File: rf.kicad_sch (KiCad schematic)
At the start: 1 part, among them U3 RFM95W-868S2

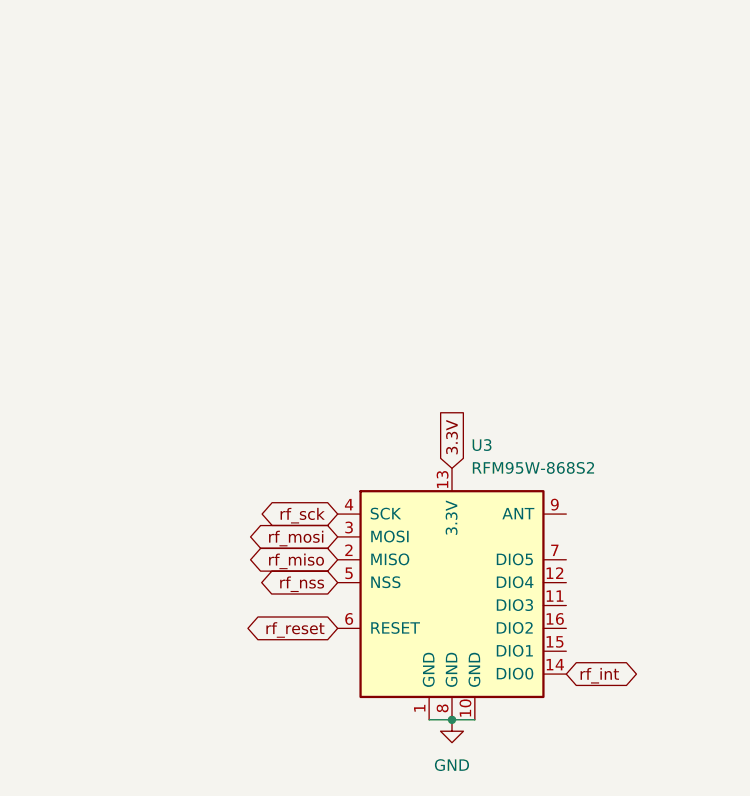
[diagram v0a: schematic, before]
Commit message: Overhaul
Overhauled the schematic so all the components are correct, rewired power to be 12 V instead of 9 V and connected hierarchical labels between modules. Added more decoupling capacitors where they were missing.
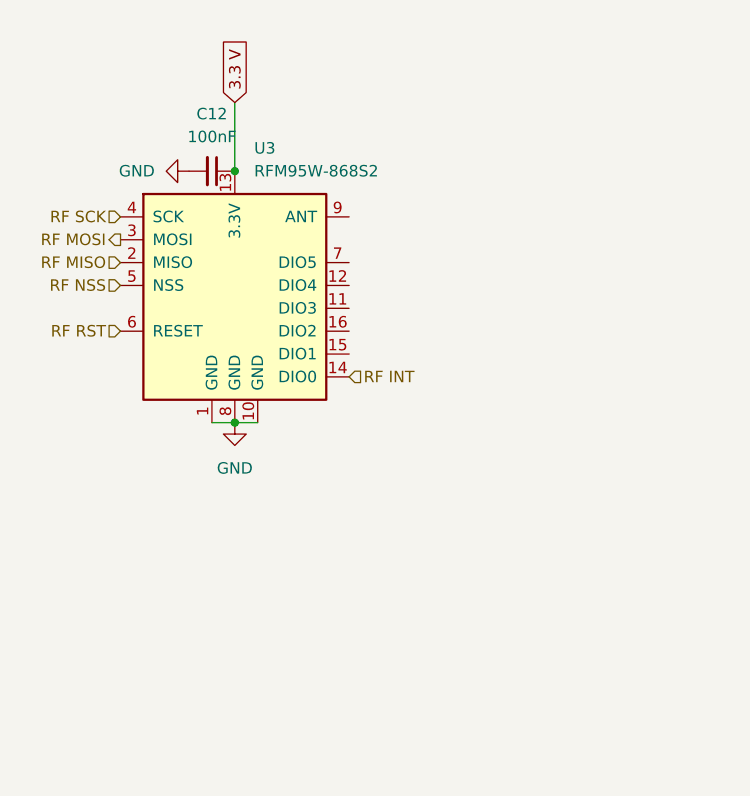
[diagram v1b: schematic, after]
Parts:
- added C12: 100nF, symbol Device:C_Small
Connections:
- net GND: now also C12.2
- net 3.3V renamed 3.3 V
- net 3.3 V: now also C12.1
- net rf_int renamed RF INT
- net rf_miso renamed RF MISO
- net rf_mosi renamed RF MOSI
- net rf_nss renamed RF NSS
- net rf_reset renamed RF RST
- net rf_sck renamed RF SCK
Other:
- moved on the sheet: U3

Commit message: Clean up
Minor fixes to mistakes in the schematic
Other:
- moved on the sheet: C12, U3
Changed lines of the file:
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@@
 	(paper "A4")
 	(junction
-		(at 41.91 57.15)
+		(at 41.91 60.96)
 		(diameter 0)
 		(color 0 0 0 0)
 	)
 	(junction
-		(at 41.91 29.21)
+		(at 41.91 31.75)
 		(diameter 0)
 		(color 0 0 0 0)
@@
 	(wire
 		(pts
-			(xy 41.91 21.59) (xy 41.91 29.21)
+			(xy 41.91 24.13) (xy 41.91 31.75)
 		)
 		(stroke
@@
 	(wire
 		(pts
-			(xy 39.37 57.15) (xy 41.91 57.15)
+			(xy 39.37 60.96) (xy 41.91 60.96)
 		)
 		(stroke
@@
 	(wire
 		(pts
-			(xy 41.91 57.15) (xy 44.45 57.15)
+			(xy 41.91 31.75) (xy 41.91 33.02)
 		)
 		(stroke
@@
 		)
 	)
+	(wire
+		(pts
+			(xy 41.91 60.96) (xy 44.45 60.96)
+		)
+		(stroke
+			(width 0)
+			(type default)
+		)
+	)
 	(global_label "3.3 V"
 		(shape input)
-		(at 41.91 21.59 90)
+		(at 41.91 24.13 90)
 		(fields_autoplaced yes)
 		(effects
@@
 		)
 		(property "Intersheetrefs" "${INTERSHEET_REFS}"
-			(at 41.91 13.5248 90)
+			(at 41.91 16.0648 90)
 			(hide yes)
 			(show_name no)
@@
 	(hierarchical_label "RF NSS"
 		(shape input)
-		(at 29.21 41.91 180)
+		(at 29.21 45.72 180)
 		(effects
 			(font
@@
 	(hierarchical_label "RF SCK"
 		(shape input)
-		(at 29.21 34.29 180)
+		(at 29.21 38.1 180)
 		(effects
 			(font
@@
 	(hierarchical_label "RF MISO"
 		(shape input)
-		(at 29.21 39.37 180)
+		(at 29.21 43.18 180)
 		(effects
 			(font
@@
 	(hierarchical_label "RF MOSI"
 		(shape output)
-		(at 29.21 36.83 180)
+		(at 29.21 40.64 180)
 		(effects
 			(font
@@
 	(hierarchical_label "RF INT"
 		(shape input)
-		(at 54.61 52.07 0)
+		(at 54.61 55.88 0)
 		(effects
 			(font
@@
 	(hierarchical_label "RF RST"
 		(shape input)
-		(at 29.21 46.99 180)
+		(at 29.21 50.8 180)
 		(effects
 			(font
@@
 	(symbol
 		(lib_id "Device:C_Small")
-		(at 39.37 29.21 270)
+		(at 39.37 31.75 270)
 		(unit 1)
 		(body_style 1)
@@
 		(fields_autoplaced yes)
 		(property "Reference" "C12"
-			(at 39.3636 22.86 90)
+			(at 39.3636 25.4 90)
 			(show_name no)
 			(do_not_autoplace no)
@@
 		)
 		(property "Value" "100nF"
-			(at 39.3636 25.4 90)
+			(at 39.3636 27.94 90)
 			(show_name no)
 			(do_not_autoplace no)
@@
 		)
 		(property "Footprint" ""
-			(at 39.37 29.21 0)
+			(at 39.37 31.75 0)
 			(hide yes)
 			(show_name no)
@@
 		)
 		(property "Datasheet" ""
-			(at 39.37 29.21 0)
+			(at 39.37 31.75 0)
 			(hide yes)
 			(show_name no)
@@
 		)
 		(property "Description" "Unpolarized capacitor, small symbol"
-			(at 39.37 29.21 0)
+			(at 39.37 31.75 0)
 			(hide yes)
 			(show_name no)
@@
 	(symbol
 		(lib_id "power:GND")
-		(at 41.91 57.15 0)
+		(at 41.91 60.96 0)
 		(unit 1)
 		(body_style 1)
@@
 		(fields_autoplaced yes)
 		(property "Reference" "#PWR011"
-			(at 41.91 63.5 0)
+			(at 41.91 67.31 0)
 			(hide yes)
 			(show_name no)
@@
 		)
 		(property "Value" "GND"
-			(at 41.91 62.23 0)
+			(at 41.91 66.04 0)
 			(show_name no)
 			(do_not_autoplace no)
@@
 		)
 		(property "Footprint" ""
-			(at 41.91 57.15 0)
+			(at 41.91 60.96 0)
 			(hide yes)
 			(show_name no)
@@
 		)
 		(property "Datasheet" ""
-			(at 41.91 57.15 0)
+			(at 41.91 60.96 0)
 			(hide yes)
 			(show_name no)
@@
 		)
 		(property "Description" "Power symbol creates a global label with name \"GND\" , ground"
-			(at 41.91 57.15 0)
+			(at 41.91 60.96 0)
 			(hide yes)
 			(show_name no)
@@
 	(symbol
 		(lib_id "power:GND")
-		(at 36.83 29.21 270)
+		(at 36.83 31.75 270)
 		(unit 1)
 		(body_style 1)
@@
 		(fields_autoplaced yes)
 		(property "Reference" "#PWR017"
-			(at 30.48 29.21 0)
+			(at 30.48 31.75 0)
 			(hide yes)
 			(show_name no)
@@
 		)
 		(property "Value" "GND"
-			(at 33.02 29.2099 90)
+			(at 33.02 31.7499 90)
 			(show_name no)
 			(do_not_autoplace no)
@@
 		)
 		(property "Footprint" ""
-			(at 36.83 29.21 0)
+			(at 36.83 31.75 0)
 			(hide yes)
 			(show_name no)
@@
 		)
 		(property "Datasheet" ""
-			(at 36.83 29.21 0)
+			(at 36.83 31.75 0)
 			(hide yes)
 			(show_name no)
@@
 		)
 		(property "Description" "Power symbol creates a global label with name \"GND\" , ground"
-			(at 36.83 29.21 0)
+			(at 36.83 31.75 0)
 			(hide yes)
 			(show_name no)
@@
 	(symbol
 		(lib_id "RF_Module:RFM95W-868S2")
-		(at 41.91 41.91 0)
+		(at 41.91 45.72 0)
 		(unit 1)
 		(body_style 1)
@@
 		(fields_autoplaced yes)
 		(property "Reference" "U3"
-			(at 44.0533 26.67 0)
+			(at 44.0533 30.48 0)
 			(show_name no)
 			(do_not_autoplace no)
@@
 		)
 		(property "Value" "RFM95W-868S2"
-			(at 44.0533 29.21 0)
+			(at 44.0533 33.02 0)
 			(show_name no)
 			(do_not_autoplace no)
@@
 		)
 		(property "Footprint" ""
-			(at -41.91 0 0)
+			(at -41.91 3.81 0)
 			(hide yes)
 			(show_name no)
@@
 		)
 		(property "Datasheet" "https://www.hoperf.com/data/upload/portal/20181127/5bfcbea20e9ef.pdf"
-			(at -41.91 0 0)
+			(at -41.91 3.81 0)
 			(hide yes)
 			(show_name no)
@@
 		)
 		(property "Description" "Low power long range transceiver module, SPI and parallel interface, 868 MHz, spreading factor 6 to12, bandwidth 7.8 to 500kHz, -111 to -148 dBm, SMD-16, DIP-16"
-			(at 41.91 41.91 0)
-			(hide yes)
-			(show_name no)
+			(at 41.91 45.72 0)
+			(hide yes)
+			(show_name no)

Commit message: Gave footprints to everything
Footprints
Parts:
- C12: footprint (none) -> Capacitor_SMD:C_0603_1608Metric
- U3: footprint (none) -> customrf:rf module
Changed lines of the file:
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@@
 			)
 		)
-		(property "Footprint" ""
+		(property "Footprint" "Capacitor_SMD:C_0603_1608Metric"
 			(at 39.37 31.75 0)
 			(hide yes)
@@
 			)
 		)
-		(property "Footprint" ""
+		(property "Footprint" "customrf:rf module"
 			(at -41.91 3.81 0)
 			(hide yes)

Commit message: Custom RF module and component
Created my own setup for the footprint for the custom RF module
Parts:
- removed U3: RFM95W-868S2, customrf:rf module, symbol RF_Module:RFM95W-868S2
- added U1: (no value), customrf:rf module, symbol X19-Float-Board-eagle-import:rfm95adafruitmodule
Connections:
- net 3.3 V: now also U1.6 (VIN)
- net GND: now also U1.7 (GND)
- net RF INT: now also U1.9 (G0)
- net RF MISO: now also U1.11 (MISO)
- net RF MOSI: now also U1.12 (MOSI)
- net RF NSS: now also U1.13 (CS)
- net RF RST: now also U1.14 (RST)
- net RF SCK: now also U1.10 (SCK)
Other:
- moved on the sheet: C12

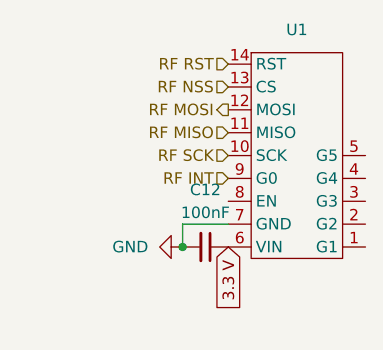
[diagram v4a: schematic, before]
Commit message: USB-C + Complete wiring
Compltetly wired the pcb (I don't understand the DRC errors) and added a usb C to flash the stm, modified the switch to be the BOOT0 for the stm so it controls whether the stm is in flash mode
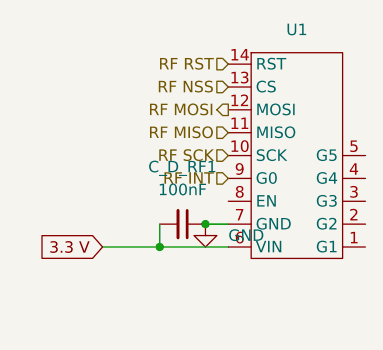
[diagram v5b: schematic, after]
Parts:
- renumbered C12 to C_D_RF1
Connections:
- net 3.3 V: now also C_D_RF1.2; no longer C_D_RF1.1
- net GND: now also C_D_RF1.1; no longer C_D_RF1.2
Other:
- moved on the sheet: C_D_RF1
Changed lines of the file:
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@@
 	(paper "A4")
 	(junction
-		(at 76.2 58.42)
+		(at 78.74 55.88)
 		(diameter 0)
 		(color 0 0 0 0)
 	)
+	(junction
+		(at 73.66 58.42)
+		(diameter 0)
+		(color 0 0 0 0)
+	)
 	(wire
 		(pts
-			(xy 76.2 58.42) (xy 76.2 55.88)
+			(xy 73.66 55.88) (xy 73.66 58.42)
 		)
 		(stroke
@@
 	(wire
 		(pts
-			(xy 76.2 55.88) (xy 81.28 55.88)
+			(xy 73.66 58.42) (xy 81.28 58.42)
 		)
 		(stroke
@@
 		)
 	)
+	(wire
+		(pts
+			(xy 67.31 58.42) (xy 73.66 58.42)
+		)
+		(stroke
+			(width 0)
+			(type default)
+		)
+	)
+	(wire
+		(pts
+			(xy 78.74 55.88) (xy 81.28 55.88)
+		)
+		(stroke
+			(width 0)
+			(type default)
+		)
+	)
 	(global_label "3.3 V"
 		(shape input)
-		(at 81.28 58.42 270)
+		(at 67.31 58.42 180)
 		(fields_autoplaced yes)
 		(effects
@@
 		)
 		(property "Intersheetrefs" "${INTERSHEET_REFS}"
-			(at 81.28 66.4852 90)
+			(at 59.2448 58.42 0)
 			(hide yes)
 			(show_name no)
@@
 	(symbol
 		(lib_id "Device:C_Small")
-		(at 78.74 58.42 270)
+		(at 76.2 55.88 270)
 		(unit 1)
 		(body_style 1)
@@
 		(dnp no)
 		(fields_autoplaced yes)
-		(property "Reference" "C12"
-			(at 78.7336 52.07 90)
+		(property "Reference" "C_D_RF1"
+			(at 76.1936 49.53 90)
 			(show_name no)
 			(do_not_autoplace no)
@@
 		)
 		(property "Value" "100nF"
-			(at 78.7336 54.61 90)
+			(at 76.1936 52.07 90)
 			(show_name no)
 			(do_not_autoplace no)
@@
 		)
 		(property "Footprint" "Capacitor_SMD:C_0603_1608Metric"
-			(at 78.74 58.42 0)
+			(at 76.2 55.88 0)
 			(hide yes)
 			(show_name no)
@@
 		)
 		(property "Datasheet" ""
-			(at 78.74 58.42 0)
+			(at 76.2 55.88 0)
 			(hide yes)
 			(show_name no)
@@
 		)
 		(property "Description" "Unpolarized capacitor, small symbol"
-			(at 78.74 58.42 0)
+			(at 76.2 55.88 0)
 			(hide yes)
 			(show_name no)
@@
 			(project "X19-Float-Board"
 				(path "/00000000-0000-0000-0000-000060e6118b/c07ea2df-4373-423b-99f3-52af8b77a578"
-					(reference "C12")
+					(reference "C_D_RF1")
 					(unit 1)
 				)
@@
 	(symbol
 		(lib_id "power:GND")
-		(at 76.2 58.42 270)
+		(at 78.74 55.88 0)
 		(unit 1)
 		(body_style 1)
@@
 		(fields_autoplaced yes)
 		(property "Reference" "#PWR017"
-			(at 69.85 58.42 0)
+			(at 78.74 62.23 0)
 			(hide yes)
 			(show_name no)
@@
 		)
 		(property "Value" "GND"
-			(at 72.39 58.4199 90)
-			(show_name no)
-			(do_not_autoplace no)
-			(effects
-				(font
-					(size 1.27 1.27)
-				)
-				(justify right)
+			(at 81.28 57.1499 0)
+			(show_name no)
+			(do_not_autoplace no)
+			(effects
+				(font
+					(size 1.27 1.27)
+				)
+				(justify left)
 			)
 		)
 		(property "Footprint" ""
-			(at 76.2 58.42 0)
+			(at 78.74 55.88 0)
 			(hide yes)
 			(show_name no)
@@
 		)
 		(property "Datasheet" ""
-			(at 76.2 58.42 0)
+			(at 78.74 55.88 0)
 			(hide yes)
 			(show_name no)
@@
 		)
 		(property "Description" "Power symbol creates a global label with name \"GND\" , ground"
-			(at 76.2 58.42 0)
-			(hide yes)
-			(show_name no)
+			(at 78.74 55.88 0)
+			(hide yes)
+			(show_name no)

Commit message: Updated Schematic
Updated parts of todo list for schematic
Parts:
- U1: footprint customrf:rf module -> CustomFootprints:rf module
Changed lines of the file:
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@@
 			)
 		)
-		(property "Footprint" "customrf:rf module"
+		(property "Footprint" "CustomFootprints:rf module"
 			(at 88.9 48.26 0)
 			(hide yes)

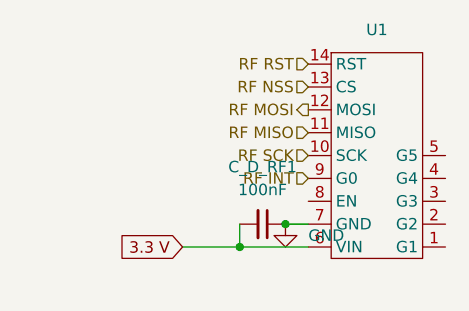
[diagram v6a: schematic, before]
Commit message: Updated Schematic
Updated schematic
Cleaned up dense portions
added H bridge
correct i2c wiring
added ferrite beads
added 12 V power monitoring
added stlink
added power mux
added power from usb
reformatted hierarichal sheets
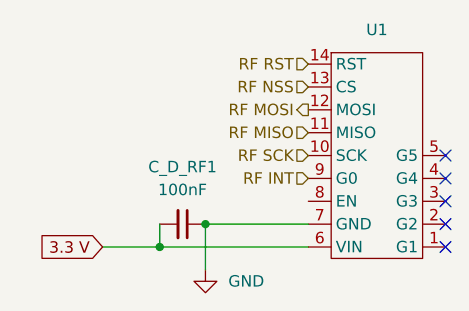
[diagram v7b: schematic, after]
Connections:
- no-connect marks 0 -> 5
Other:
- moved on the sheet: C_D_RF1
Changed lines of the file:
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@@
 	(paper "A4")
 	(junction
-		(at 78.74 55.88)
+		(at 64.77 58.42)
 		(diameter 0)
 		(color 0 0 0 0)
 	)
 	(junction
-		(at 73.66 58.42)
+		(at 69.85 55.88)
 		(diameter 0)
 		(color 0 0 0 0)
 	)
-	(wire
-		(pts
-			(xy 73.66 55.88) (xy 73.66 58.42)
-		)
-		(stroke
-			(width 0)
-			(type default)
-		)
-	)
-	(wire
-		(pts
-			(xy 73.66 58.42) (xy 81.28 58.42)
-		)
-		(stroke
-			(width 0)
-			(type default)
-		)
-	)
-	(wire
-		(pts
-			(xy 67.31 58.42) (xy 73.66 58.42)
-		)
-		(stroke
-			(width 0)
-			(type default)
-		)
-	)
-	(wire
-		(pts
-			(xy 78.74 55.88) (xy 81.28 55.88)
+	(no_connect
+		(at 96.52 58.42)
+	)
+	(no_connect
+		(at 96.52 50.8)
+	)
+	(no_connect
+		(at 96.52 55.88)
+	)
+	(no_connect
+		(at 96.52 48.26)
+	)
+	(no_connect
+		(at 96.52 53.34)
+	)
+	(wire
+		(pts
+			(xy 69.85 60.96) (xy 69.85 55.88)
+		)
+		(stroke
+			(width 0)
+			(type default)
+		)
+	)
+	(wire
+		(pts
+			(xy 64.77 55.88) (xy 64.77 58.42)
+		)
+		(stroke
+			(width 0)
+			(type default)
+		)
+	)
+	(wire
+		(pts
+			(xy 64.77 58.42) (xy 81.28 58.42)
+		)
+		(stroke
+			(width 0)
+			(type default)
+		)
+	)
+	(wire
+		(pts
+			(xy 58.42 58.42) (xy 64.77 58.42)
+		)
+		(stroke
+			(width 0)
+			(type default)
+		)
+	)
+	(wire
+		(pts
+			(xy 69.85 55.88) (xy 81.28 55.88)
 		)
 		(stroke
@@
 	(global_label "3.3 V"
 		(shape input)
-		(at 67.31 58.42 180)
+		(at 58.42 58.42 180)
 		(fields_autoplaced yes)
 		(effects
@@
 		)
 		(property "Intersheetrefs" "${INTERSHEET_REFS}"
-			(at 59.2448 58.42 0)
+			(at 50.3548 58.42 0)
 			(hide yes)
 			(show_name no)
@@
 	(symbol
 		(lib_id "Device:C_Small")
-		(at 76.2 55.88 270)
+		(at 67.31 55.88 270)
 		(unit 1)
 		(body_style 1)
@@
 		(fields_autoplaced yes)
 		(property "Reference" "C_D_RF1"
-			(at 76.1936 49.53 90)
+			(at 67.3036 49.53 90)
 			(show_name no)
 			(do_not_autoplace no)
@@
 		)
 		(property "Value" "100nF"
-			(at 76.1936 52.07 90)
+			(at 67.3036 52.07 90)
 			(show_name no)
 			(do_not_autoplace no)
@@
 		)
 		(property "Footprint" "Capacitor_SMD:C_0603_1608Metric"
-			(at 76.2 55.88 0)
+			(at 67.31 55.88 0)
 			(hide yes)
 			(show_name no)
@@
 		)
 		(property "Datasheet" ""
-			(at 76.2 55.88 0)
+			(at 67.31 55.88 0)
 			(hide yes)
 			(show_name no)
@@
 		)
 		(property "Description" "Unpolarized capacitor, small symbol"
-			(at 76.2 55.88 0)
+			(at 67.31 55.88 0)
 			(hide yes)
 			(show_name no)
@@
 	(symbol
 		(lib_id "power:GND")
-		(at 78.74 55.88 0)
+		(at 69.85 60.96 0)
 		(unit 1)
 		(body_style 1)
@@
 		(fields_autoplaced yes)
 		(property "Reference" "#PWR017"
-			(at 78.74 62.23 0)
+			(at 69.85 67.31 0)
 			(hide yes)
 			(show_name no)
@@
 		)
 		(property "Value" "GND"
-			(at 81.28 57.1499 0)
+			(at 72.39 62.2299 0)
 			(show_name no)
 			(do_not_autoplace no)
@@
 		)
 		(property "Footprint" ""
-			(at 78.74 55.88 0)
+			(at 69.85 60.96 0)
 			(hide yes)
 			(show_name no)
@@
 		)
 		(property "Datasheet" ""
-			(at 78.74 55.88 0)
+			(at 69.85 60.96 0)
 			(hide yes)
 			(show_name no)
@@
 		)
 		(property "Description" "Power symbol creates a global label with name \"GND\" , ground"
-			(at 78.74 55.88 0)
-			(hide yes)
-			(show_name no)
+			(at 69.85 60.96 0)
+			(hide yes)
+			(show_name no)

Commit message: USB, TVS, LDO, Passives, I2C
applied changes to usb circuitry, tvs, ldo, passibes and i2c.
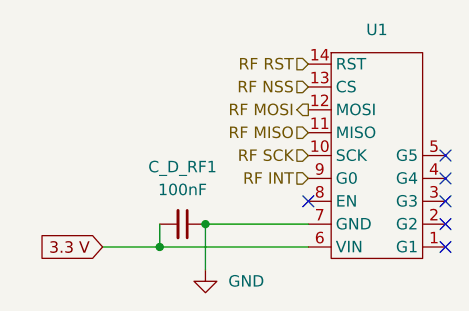
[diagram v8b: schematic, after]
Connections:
- no-connect marks 5 -> 6
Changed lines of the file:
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@@
+	)
+	(no_connect
+		(at 81.28 53.34)
 	)
 	(no_connect
